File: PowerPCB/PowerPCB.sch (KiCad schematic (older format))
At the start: 38 parts, among them J1 Conn_01x03_Male, J2 Conn_01x10_Male, J5 Conn_01x07_Male, K1 1721081-5, K2 1721081-5, U1 NCP1117-3.3_SOT223, U2 STM32F413ZHTx, U3 NCP1117-5.0_SOT223, U4 MCP2562-E-P, U5 MCP2562-E-P

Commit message: Added bypass capacitors to CAN transceivers
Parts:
- removed R9: 120, Resistor_SMD:R_0805_2012Metric_Pad1.15x1.40mm_HandSolder, symbol Device:R
- removed U5: MCP2562-E-P, Package_DIP:DIP-8_W7.62mm, symbol Interface_CAN_LIN:MCP2562-E-P
- added C5, C6, C7, C8: 0.1u, Capacitor_SMD:C_0805_2012Metric_Pad1.15x1.40mm_HandSolder, symbol Device:C
- added R2: 120, Resistor_SMD:R_0805_2012Metric_Pad1.15x1.40mm_HandSolder, symbol Device:R
- added U4: MCP2562-E-P, Package_DIP:DIP-8_W7.62mm, symbol Interface_CAN_LIN:MCP2562-E-P
- C1: renamed from C3; value C -> 0.1u
- C2: renamed from C1; value C -> 0.1u
- C3: renamed from C4; value C -> 0.1u
- C4: renamed from C2; value C -> 0.1u
- renumbered C6 to C10, C7 to C11, C8 to C12, C5 to C9, D2 to D1, D3 to D2, D4 to D3, D5 to D4, D1 to D5, J5 to J3, R3 to R1, R5 to R12, R6 to R13, R7 to R14, R12 to R3, R13 to R4, R14 to R5, R16 to R6, R1 to R7, R2 to R8, R4 to R9, U3 to U1, U1 to U2, U4 to U3, U2 to U5
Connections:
- net GND: now also C5.2, C6.2, C7.2, C8.2, U4.2 (VSS), U4.8 (STBY)
- net MAIN_CAN_HI: now also R2.1, U4.7 (CANH)
- net MAIN_CAN_LO: now also R2.2, U4.6 (CANL)
- net MAIN_CAN_RX: now also U4.4 (RXD)
- net MAIN_CAN_TX: now also U4.1 (TXD)
- net VCC_3.3: now also C5.1, C6.1, U4.5 (Vio)
- net VCC_5: now also C7.1, C8.1, U4.3 (VDD)
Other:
- moved on the sheet: C1, C2, C3, C4, U1, U2

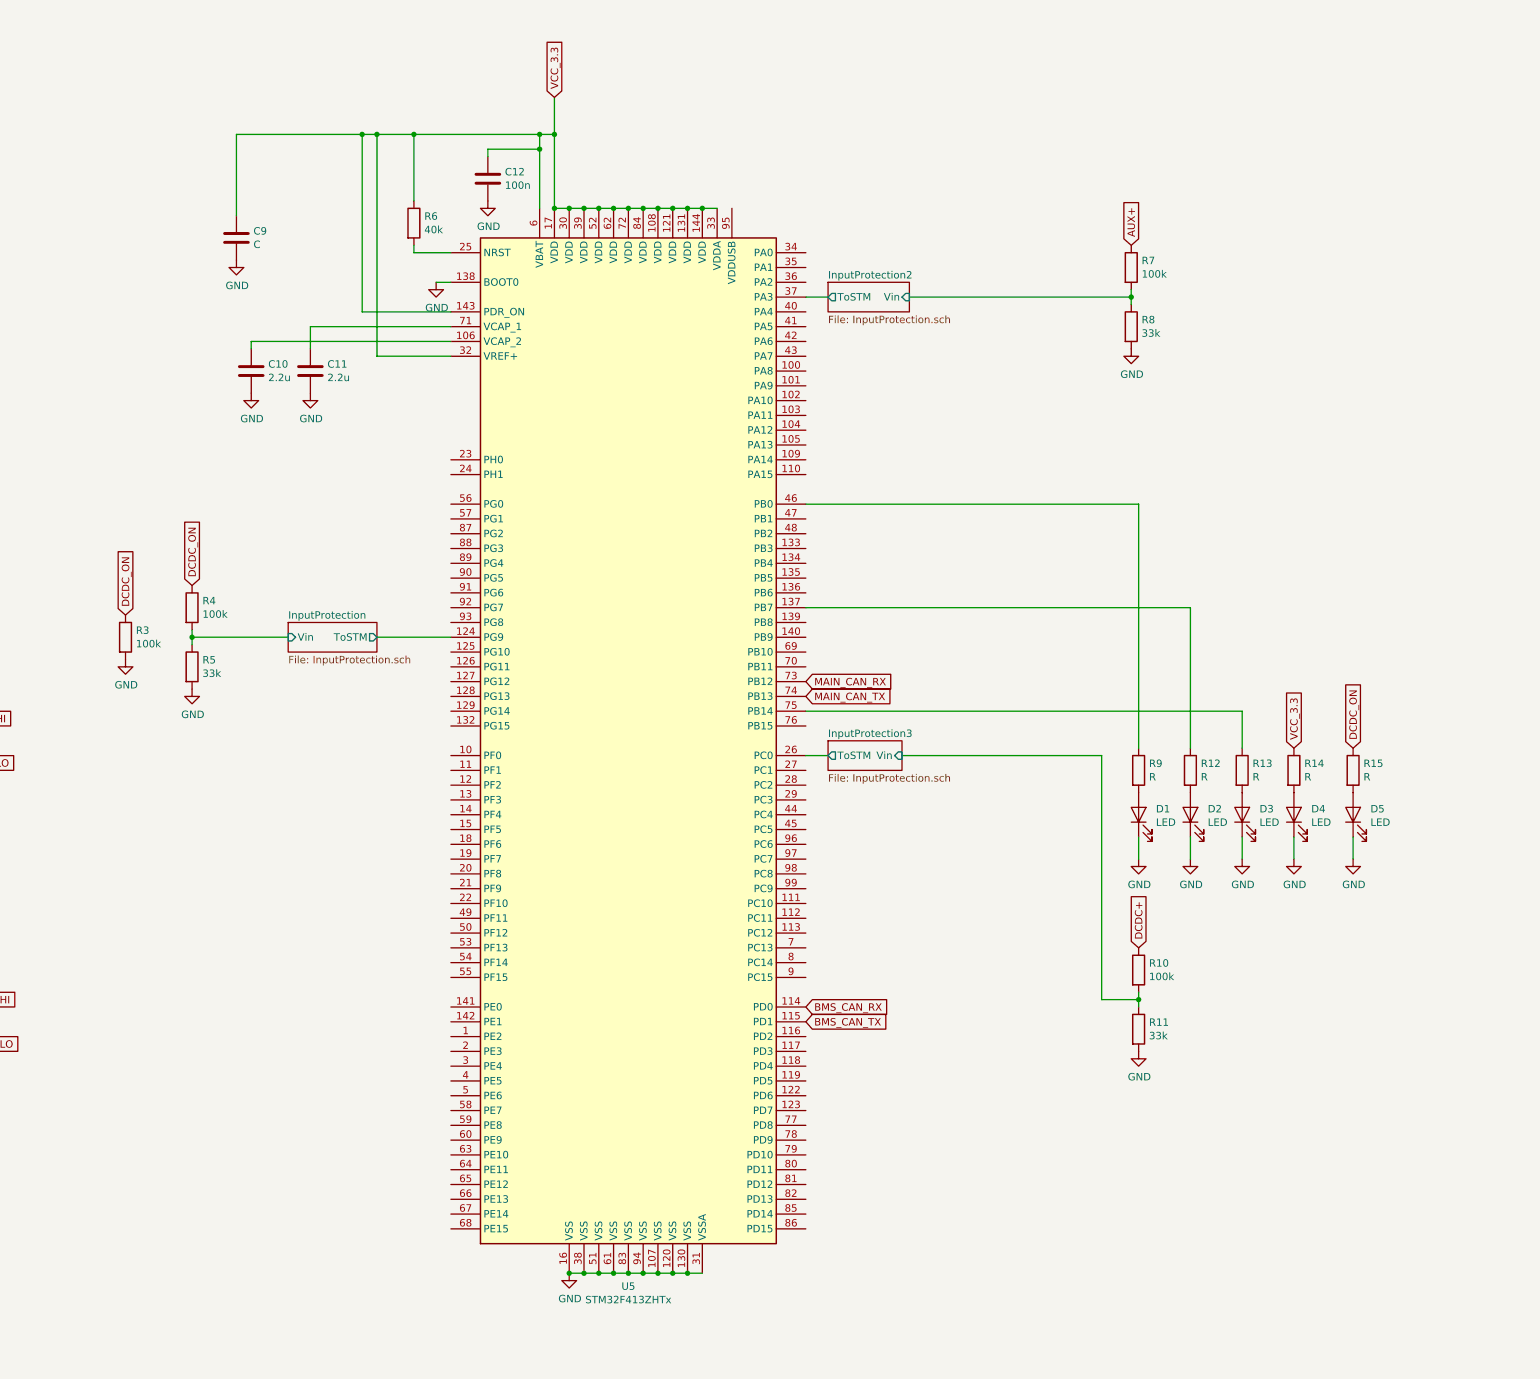
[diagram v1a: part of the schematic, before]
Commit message: Added VDD bypass capacitors and values for all components
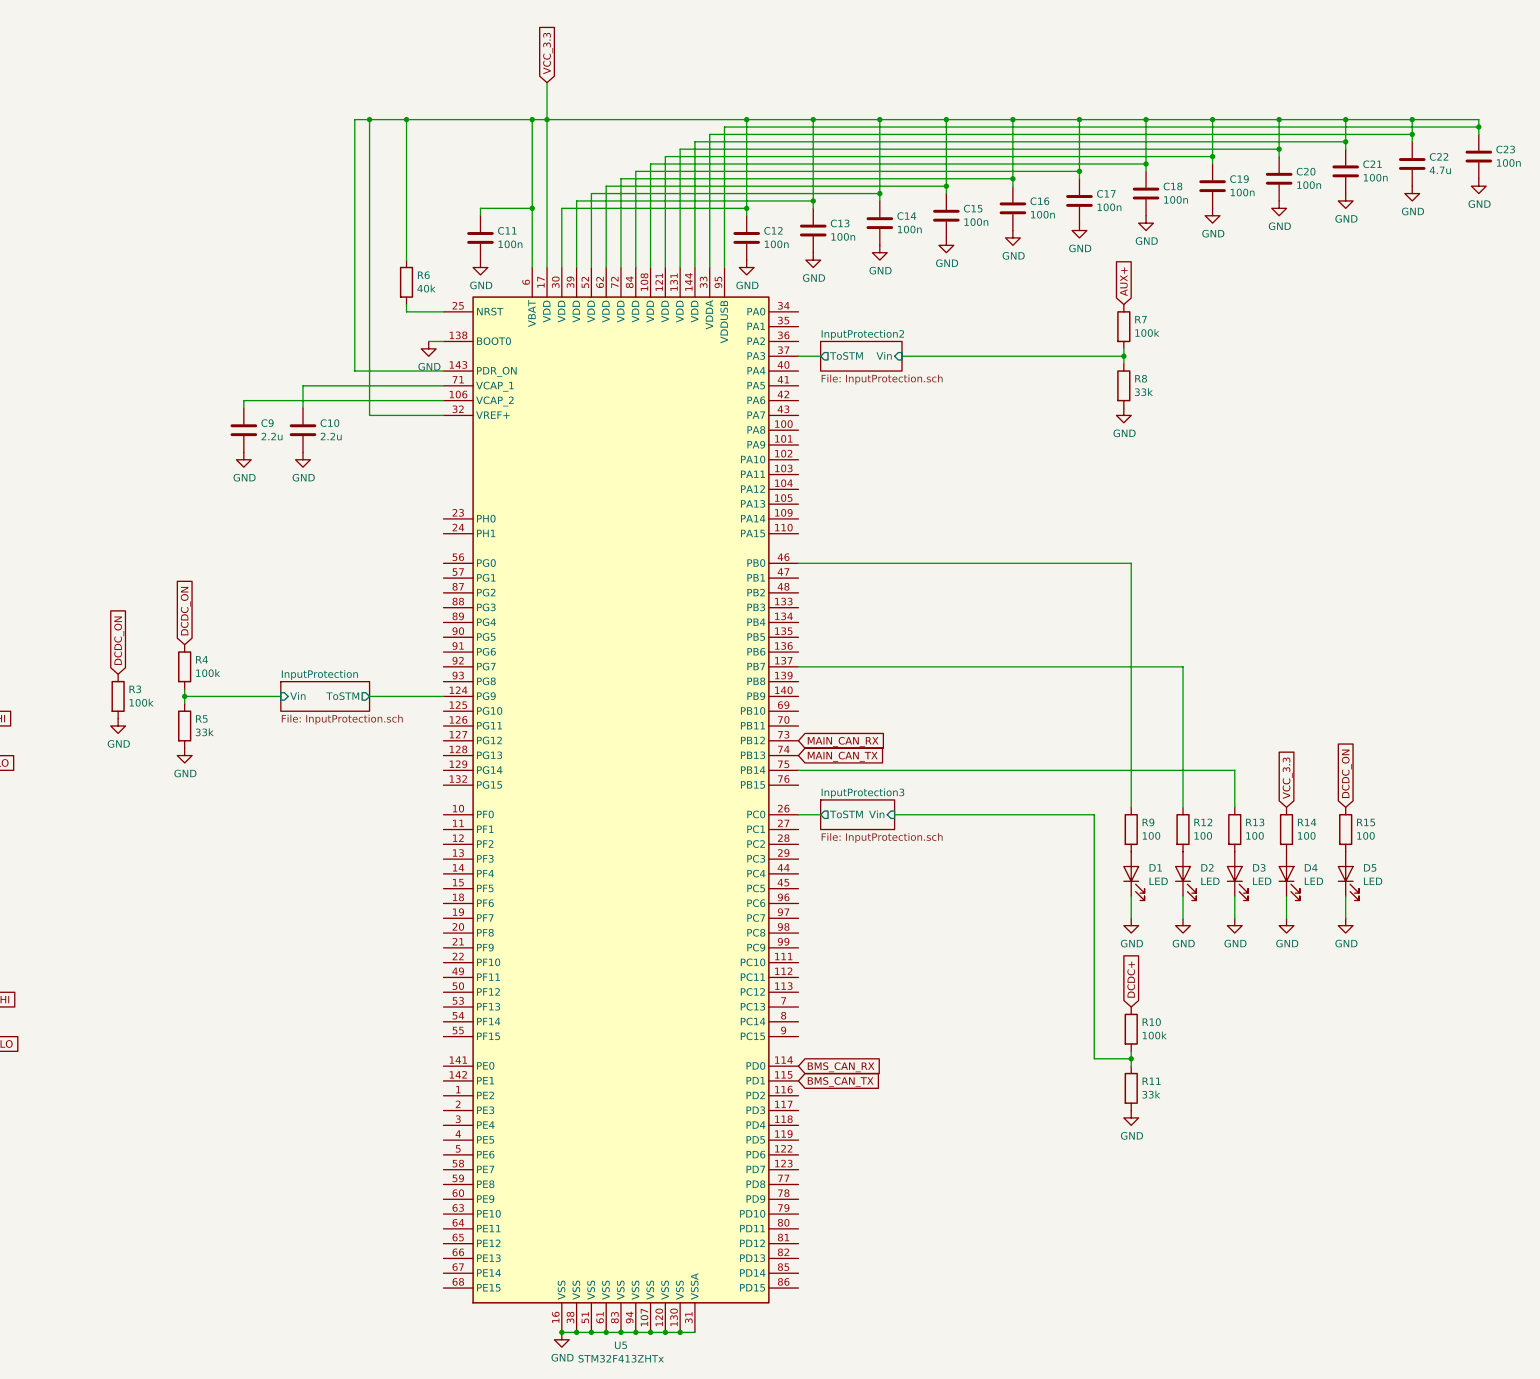
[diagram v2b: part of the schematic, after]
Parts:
- added C13, C14, C15, C16, C17, C18, C19, C20, C21, C23: 100n, Capacitor_SMD:C_0805_2012Metric_Pad1.15x1.40mm_HandSolder, symbol Device:C
- added C22: 4.7u, Capacitor_SMD:C_0805_2012Metric_Pad1.15x1.40mm_HandSolder, symbol Device:C
- C12: renamed from C9; value C -> 100n
- R12, R13, R14, R15, R9: value R -> 100
- renumbered C11 to C10, C12 to C11, C10 to C9
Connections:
- net GND: now also C13.2, C14.2, C15.2, C16.2, C17.2, C18.2, C19.2, C20.2, C21.2, C22.2, C23.2
- net VCC_3.3: now also U5.95 (VDDUSB), C13.1, C14.1, C15.1, C16.1, C17.1, C18.1, C19.1, C20.1, C21.1, C22.1, C23.1
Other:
- moved on the sheet: C10, C11, C12, C9, D1, D2, D3, D4, D5, R10, R11, R12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

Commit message: Added pull-down resistors to usused pins
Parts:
- renumbered C5 to C10, C6 to C11, C14 to C12, C15 to C13, C16 to C14, C7 to C15, C8 to C16, C9 to C3, C3 to C4, C4 to C5, C10 to C6, C11 to C7, C12 to C8, C13 to C9, R3 to R1, R4 to R2, R5 to R3, R6 to R4, R1 to R5, R2 to R6, U5 to U3, U3 to U4, U4 to U5
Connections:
- net sheet601A1534/ToSTM: now reaches U3.1 (PE2)
- net sheet601B941E/ToSTM: now reaches U3.10 (PF0)
- net sheet5FFC3C6B/ToSTM: now reaches U3.100 (PA8)
- net sheet5FFC3C6A/ToSTM: now reaches U3.101 (PA9)
- net sheet5FFA3E10/ToSTM: now reaches U3.102 (PA10)
- net sheet5FFA3E0F/ToSTM: now reaches U3.103 (PA11)
- net sheet5FFA3E0E/ToSTM: now reaches U3.104 (PA12)
- net sheet5FFA3E0D/ToSTM: now reaches U3.105 (PA13)
- net sheet5FFA3E0C/ToSTM: now reaches U3.109 (PA14)
- net sheet601B941D/ToSTM: now reaches U3.11 (PF1)
- net sheet5FFA3E0B/ToSTM: now reaches U3.110 (PA15)
- net sheet5F9ACCA2/ToSTM: now reaches U3.111 (PC10)
- net sheet5F9ACCA3/ToSTM: now reaches U3.112 (PC11)
- net sheet5F8C41A1/ToSTM: now reaches U3.113 (PC12)
- net sheet5F7D6EC4/ToSTM: now reaches U3.116 (PD2)
- net sheet5F6ABF7E/ToSTM: now reaches U3.117 (PD3)
- net sheet5F6ABF7D/ToSTM: now reaches U3.118 (PD4)
- net sheet5F495768/ToSTM: now reaches U3.119 (PD5)
- net sheet601B941C/ToSTM: now reaches U3.12 (PF2)
- net sheet5F46D812/ToSTM: now reaches U3.122 (PD6)
- net sheet5F39C745/ToSTM: now reaches U3.123 (PD7)
- net sheet6023EBBC/ToSTM: now reaches U3.125 (PG10)
- net sheet6023EBBB/ToSTM: now reaches U3.126 (PG11)
- net sheet6023EBBA/ToSTM: now reaches U3.127 (PG12)
- net sheet6023EBB9/ToSTM: now reaches U3.128 (PG13)
- net sheet6023EBB8/ToSTM: now reaches U3.129 (PG14)
- net sheet601B941B/ToSTM: now reaches U3.13 (PF3)
- net sheet6023EBB7/ToSTM: now reaches U3.132 (PG15)
- net sheet5FF21F24/ToSTM: now reaches U3.133 (PB3)
- net sheet5FF21F23/ToSTM: now reaches U3.134 (PB4)
- net sheet5FF21F22/ToSTM: now reaches U3.135 (PB5)
- net sheet5FF21F21/ToSTM: now reaches U3.136 (PB6)
- net sheet5FEDAA52/ToSTM: now reaches U3.139 (PB8)
- net sheet601B941A/ToSTM: now reaches U3.14 (PF4)
- net sheet5FEDAA51/ToSTM: now reaches U3.140 (PB9)
- net sheet601A1536/ToSTM: now reaches U3.141 (PE0)
- net sheet601A1535/ToSTM: now reaches U3.142 (PE1)
- net sheet601B9419/ToSTM: now reaches U3.15 (PF5)
- net sheet601B9418/ToSTM: now reaches U3.18 (PF6)
- net sheet601B9417/ToSTM: now reaches U3.19 (PF7)
- net sheet601A1533/ToSTM: now reaches U3.2 (PE3)
- net sheet601B9416/ToSTM: now reaches U3.20 (PF8)
- net sheet601B9415/ToSTM: now reaches U3.21 (PF9)
- net sheet601B9414/ToSTM: now reaches U3.22 (PF10)
- net sheet60294697/ToSTM: now reaches U3.23 (PH0)
- net sheet60294696/ToSTM: now reaches U3.24 (PH1)
- net sheet5FDB7445/ToSTM: now reaches U3.27 (PC1)
- net sheet5FDB7444/ToSTM: now reaches U3.28 (PC2)
- net sheet5FDB7443/ToSTM: now reaches U3.29 (PC3)
- net sheet601A1532/ToSTM: now reaches U3.3 (PE4)
- net sheet60007503/ToSTM: now reaches U3.34 (PA0)
- net sheet60007502/ToSTM: now reaches U3.35 (PA1)
- net sheet60007501/ToSTM: now reaches U3.36 (PA2)
- net sheet601A1531/ToSTM: now reaches U3.4 (PE5)
- net sheet5FFC3C6F/ToSTM: now reaches U3.40 (PA4)
- net sheet5FFC3C6E/ToSTM: now reaches U3.41 (PA5)
- net sheet5FFC3C6D/ToSTM: now reaches U3.42 (PA6)
- net sheet5FFC3C6C/ToSTM: now reaches U3.43 (PA7)
- net sheet5FDB7442/ToSTM: now reaches U3.44 (PC4)
- net sheet5FDB7441/ToSTM: now reaches U3.45 (PC5)
- net sheet5FF21F26/ToSTM: now reaches U3.47 (PB1)
- net sheet5FF21F25/ToSTM: now reaches U3.48 (PB2)
- net sheet601B9413/ToSTM: now reaches U3.49 (PF11)
- net sheet601A1530/ToSTM: now reaches U3.5 (PE6)
- net sheet601B9412/ToSTM: now reaches U3.50 (PF12)
- net sheet601B9411/ToSTM: now reaches U3.53 (PF13)
- net sheet601B9410/ToSTM: now reaches U3.54 (PF14)
- net sheet601B940F/ToSTM: now reaches U3.55 (PF15)
- net sheet60294695/ToSTM: now reaches U3.56 (PG0)
- net sheet60294694/ToSTM: now reaches U3.57 (PG1)
- net sheet601A152F/ToSTM: now reaches U3.58 (PE7)
- net sheet6013EBF5/ToSTM: now reaches U3.59 (PE8)
- net sheet6013EBF4/ToSTM: now reaches U3.60 (PE9)
- net sheet6013EBF3/ToSTM: now reaches U3.63 (PE10)
- net sheet6013EBF2/ToSTM: now reaches U3.64 (PE11)
- net sheet600F4DA5/ToSTM: now reaches U3.65 (PE12)
- net sheet600F4DA4/ToSTM: now reaches U3.66 (PE13)
- net sheet600D131C/ToSTM: now reaches U3.67 (PE14)
- net sheet600AE2AF/ToSTM: now reaches U3.68 (PE15)
- net sheet5FEDAA50/ToSTM: now reaches U3.69 (PB10)
- net sheet5F8C41A0/ToSTM: now reaches U3.7 (PC13)
- net sheet5FEDAA4F/ToSTM: now reaches U3.70 (PB11)
- net sheet5FE6F3ED/ToSTM: now reaches U3.76 (PB15)
- net sheet5F39C744/ToSTM: now reaches U3.77 (PD8)
- net sheet5F782635/ToSTM: now reaches U3.78 (PD9)
- net sheet5F658E1A/ToSTM: now reaches U3.79 (PD10)
- net sheet5F8C419F/ToSTM: now reaches U3.8 (PC14)
- net sheet5F5DDB0A/ToSTM: now reaches U3.80 (PD11)
- net sheet5F39C743/ToSTM: now reaches U3.81 (PD12)
- net sheet5F3495EA/ToSTM: now reaches U3.82 (PD13)
- net sheet5F3495E9/ToSTM: now reaches U3.85 (PD14)
- net sheet5F2A8D43/ToSTM: now reaches U3.86 (PD15)
- net sheet60294693/ToSTM: now reaches U3.87 (PG2)
- net sheet60294692/ToSTM: now reaches U3.88 (PG3)
- net sheet602781FC/ToSTM: now reaches U3.89 (PG4)
- net sheet5F8C419E/ToSTM: now reaches U3.9 (PC15)
- net sheet602781FB/ToSTM: now reaches U3.90 (PG5)
- net sheet602781FA/ToSTM: now reaches U3.91 (PG6)
- net sheet602781F9/ToSTM: now reaches U3.92 (PG7)
- net sheet602781F8/ToSTM: now reaches U3.93 (PG8)
- net sheet5FDB7440/ToSTM: now reaches U3.96 (PC6)
- net sheet5FDB743F/ToSTM: now reaches U3.97 (PC7)
- net sheet5FDDCD42/ToSTM: now reaches U3.98 (PC8)
- net sheet5FD6D46A/ToSTM: now reaches U3.99 (PC9)
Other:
- moved on the sheet: C1, C10, C11, C12, C13, C14, C15, C16, C17, C18, C19, C2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
